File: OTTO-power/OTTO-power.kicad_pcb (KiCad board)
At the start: 2 copper layers, 72.5 x 23.5 mm, 48 parts, among them J1 Barrel_Jack, J2 Conn_01x10, J3 USB_B_Micro, J4 battery, SW1 SW_Push, SW2 SW_reset, U1 MAX8903A, U2 MAX17048, U3 TPS61090, U4 XC6210

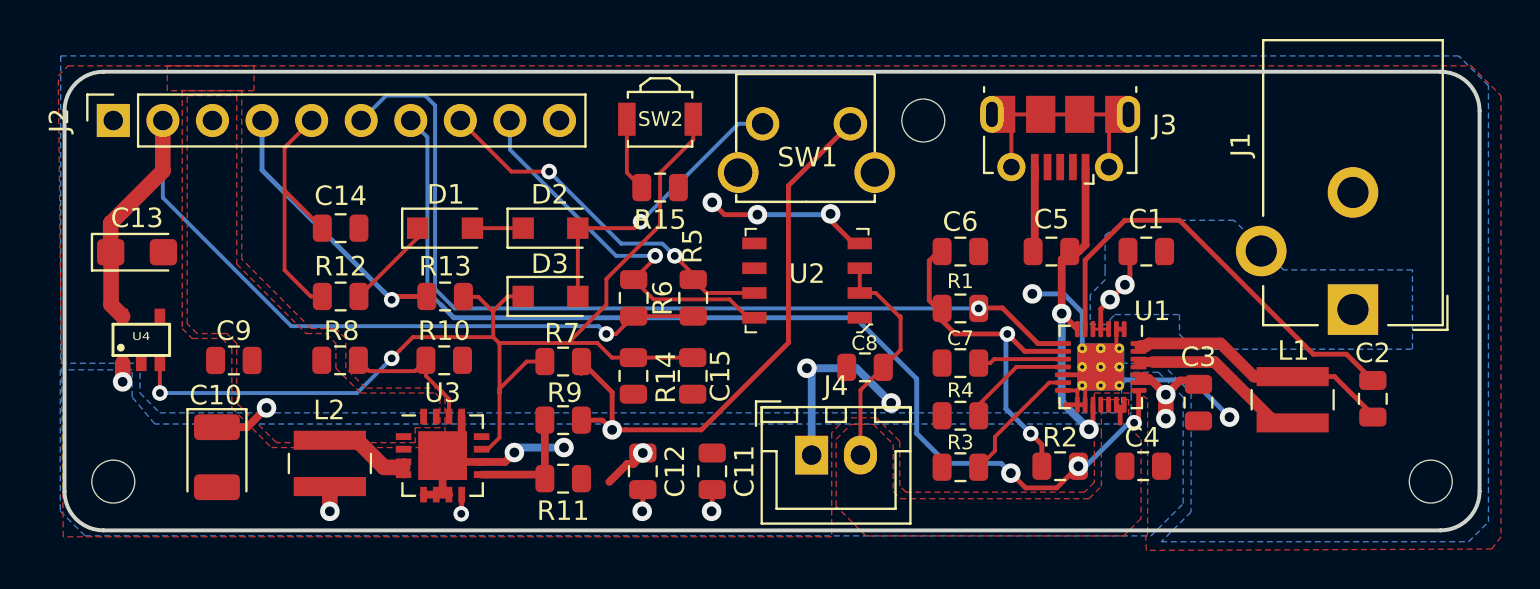
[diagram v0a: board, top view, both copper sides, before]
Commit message: added the OTTO-Keys board and fixed some of the mainboard issues
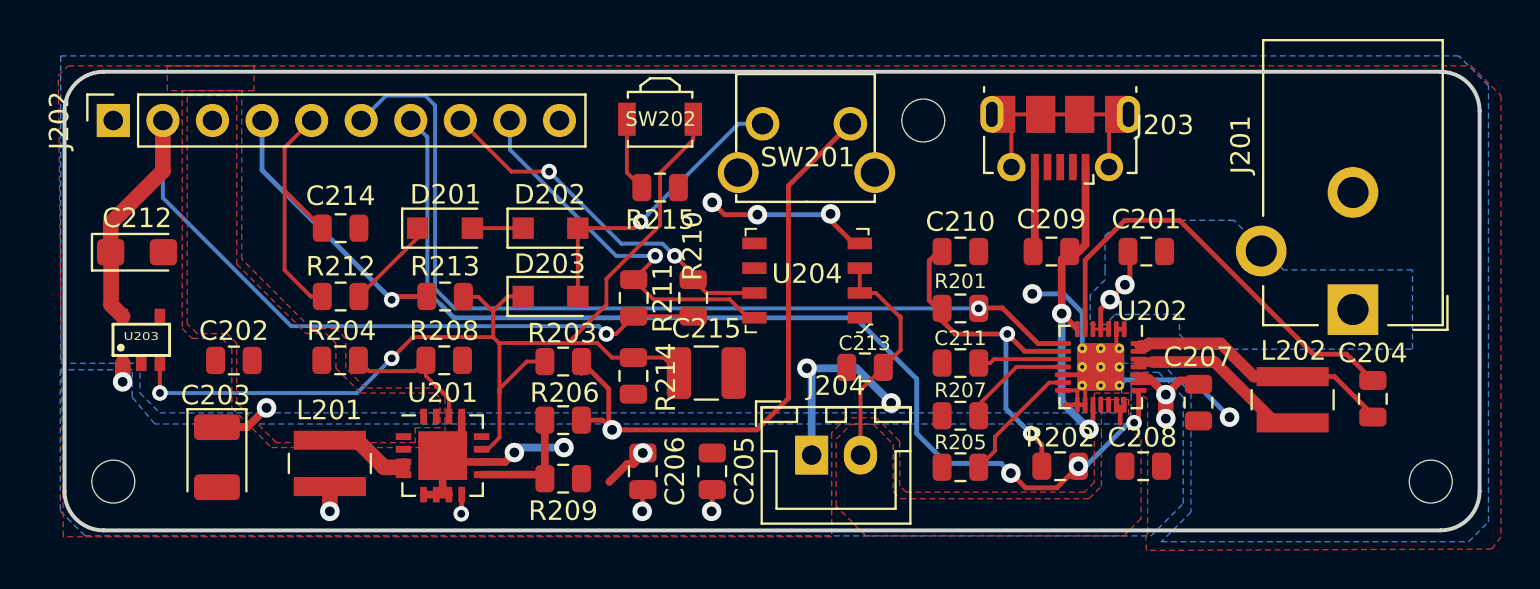
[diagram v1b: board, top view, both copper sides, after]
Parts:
- removed C15: 100uf, Capacitor_SMD:C_0805_2012Metric
- added C215: 100uf, Capacitor_SMD:C_1210_3225Metric, F.Cu at (182.4, 39.3)
- renumbered C1 to C201, C9 to C202, C10 to C203, C2 to C204, C11 to C205, C12 to C206, C3 to C207, C4 to C208, C5 to C209, C6 to C210, C7 to C211, C13 to C212, C8 to C213, C14 to C214, D1 to D201, D2 to D202, D3 to D203, J1 to J201, J2 to J202, J3 to J203, J4 to J204, L2 to L201, L1 to L202, R1 to R201, R2 to R202, R7 to R203, R8 to R204, R3 to R205, R9 to R206, R4 to R207, R10 to R208, R11 to R209, R5 to R210, R6 to R211, R12 to R212, R13 to R213, R14 to R214, R15 to R215, SW1 to SW201, SW2 to SW202, U3 to U201, U1 to U202, U4 to U203, U2 to U204
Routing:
- net SYS: track 43.1 -> 44.7 mm
